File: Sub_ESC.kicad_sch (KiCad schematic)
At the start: 2 parts

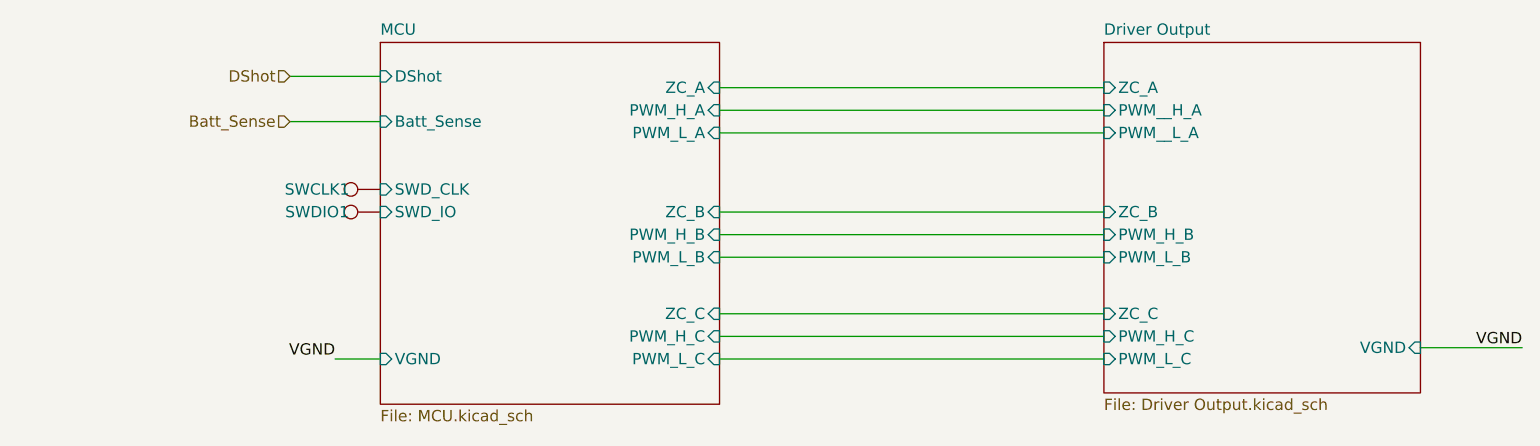
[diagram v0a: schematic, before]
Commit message: Fixed pin names
reset pins to apply proper net names
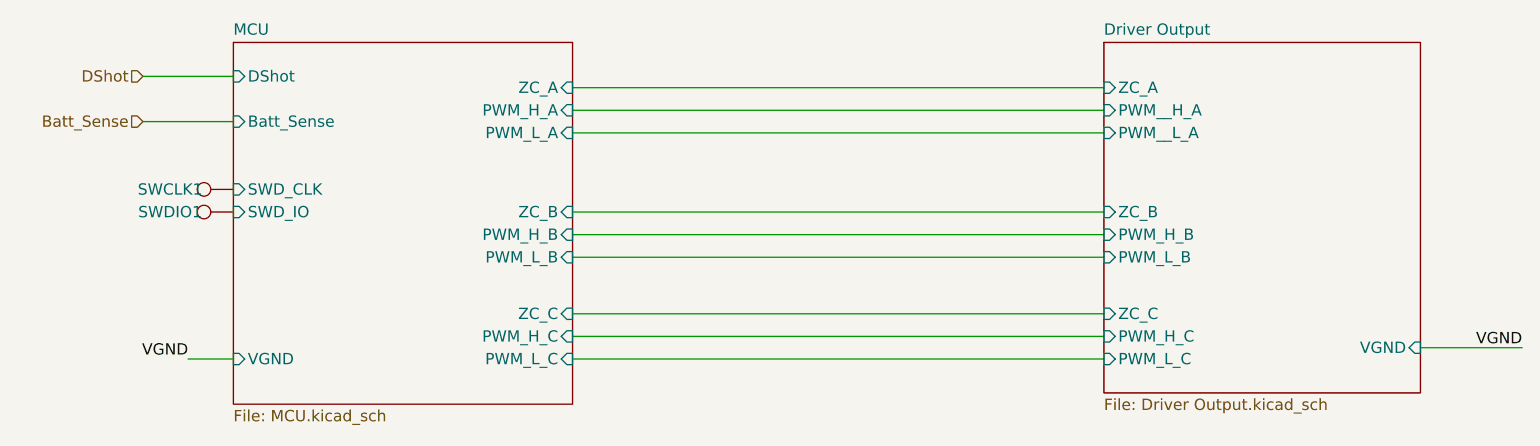
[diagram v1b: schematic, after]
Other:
- moved on the sheet: SWCLK1, SWDIO1
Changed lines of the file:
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@@
 	(wire
 		(pts
-			(xy 132.08 110.49) (xy 175.26 110.49)
-		)
-		(stroke
-			(width 0)
-			(type default)
-		)
-	)
-	(wire
-		(pts
-			(xy 132.08 82.55) (xy 175.26 82.55)
-		)
-		(stroke
-			(width 0)
-			(type default)
-		)
-	)
-	(wire
-		(pts
-			(xy 132.08 80.01) (xy 175.26 80.01)
-		)
-		(stroke
-			(width 0)
-			(type default)
-		)
-	)
-	(wire
-		(pts
-			(xy 132.08 85.09) (xy 175.26 85.09)
-		)
-		(stroke
-			(width 0)
-			(type default)
-		)
-	)
-	(wire
-		(pts
-			(xy 132.08 99.06) (xy 175.26 99.06)
-		)
-		(stroke
-			(width 0)
-			(type default)
-		)
-	)
-	(wire
-		(pts
-			(xy 132.08 105.41) (xy 175.26 105.41)
-		)
-		(stroke
-			(width 0)
-			(type default)
-		)
-	)
-	(wire
-		(pts
-			(xy 88.9 110.49) (xy 93.98 110.49)
-		)
-		(stroke
-			(width 0)
-			(type default)
-		)
-	)
-	(wire
-		(pts
-			(xy 132.08 96.52) (xy 175.26 96.52)
-		)
-		(stroke
-			(width 0)
-			(type default)
-		)
-	)
-	(wire
-		(pts
-			(xy 83.82 78.74) (xy 93.98 78.74)
-		)
-		(stroke
-			(width 0)
-			(type default)
-		)
-	)
-	(wire
-		(pts
-			(xy 132.08 107.95) (xy 175.26 107.95)
-		)
-		(stroke
-			(width 0)
-			(type default)
-		)
-	)
-	(wire
-		(pts
-			(xy 132.08 93.98) (xy 175.26 93.98)
-		)
-		(stroke
-			(width 0)
-			(type default)
-		)
-	)
-	(wire
-		(pts
-			(xy 83.82 83.82) (xy 93.98 83.82)
+			(xy 115.57 110.49) (xy 175.26 110.49)
+		)
+		(stroke
+			(width 0)
+			(type default)
+		)
+	)
+	(wire
+		(pts
+			(xy 115.57 82.55) (xy 175.26 82.55)
+		)
+		(stroke
+			(width 0)
+			(type default)
+		)
+	)
+	(wire
+		(pts
+			(xy 115.57 80.01) (xy 175.26 80.01)
+		)
+		(stroke
+			(width 0)
+			(type default)
+		)
+	)
+	(wire
+		(pts
+			(xy 115.57 85.09) (xy 175.26 85.09)
+		)
+		(stroke
+			(width 0)
+			(type default)
+		)
+	)
+	(wire
+		(pts
+			(xy 115.57 99.06) (xy 175.26 99.06)
+		)
+		(stroke
+			(width 0)
+			(type default)
+		)
+	)
+	(wire
+		(pts
+			(xy 115.57 105.41) (xy 175.26 105.41)
+		)
+		(stroke
+			(width 0)
+			(type default)
+		)
+	)
+	(wire
+		(pts
+			(xy 72.39 110.49) (xy 77.47 110.49)
+		)
+		(stroke
+			(width 0)
+			(type default)
+		)
+	)
+	(wire
+		(pts
+			(xy 115.57 96.52) (xy 175.26 96.52)
+		)
+		(stroke
+			(width 0)
+			(type default)
+		)
+	)
+	(wire
+		(pts
+			(xy 67.31 78.74) (xy 77.47 78.74)
+		)
+		(stroke
+			(width 0)
+			(type default)
+		)
+	)
+	(wire
+		(pts
+			(xy 115.57 107.95) (xy 175.26 107.95)
+		)
+		(stroke
+			(width 0)
+			(type default)
+		)
+	)
+	(wire
+		(pts
+			(xy 115.57 93.98) (xy 175.26 93.98)
+		)
+		(stroke
+			(width 0)
+			(type default)
+		)
+	)
+	(wire
+		(pts
+			(xy 67.31 83.82) (xy 77.47 83.82)
 		)
 		(stroke
@@
 	)
 	(label "VGND"
-		(at 88.9 110.49 180)
+		(at 72.39 110.49 180)
 		(effects
 			(font
@@
 	(hierarchical_label "DShot"
 		(shape input)
-		(at 83.82 78.74 180)
+		(at 67.31 78.74 180)
 		(effects
 			(font
@@
 	(hierarchical_label "Batt_Sense"
 		(shape input)
-		(at 83.82 83.82 180)
+		(at 67.31 83.82 180)
 		(effects
 			(font
@@
 	(symbol
 		(lib_id "Connector:TestPoint")
-		(at 93.98 91.44 90)
+		(at 77.47 91.44 90)
 		(unit 1)
 		(exclude_from_sim no)
@@
 		(dnp no)
 		(property "Reference" "SWCLK1"
-			(at 86.868 91.44 90)
+			(at 70.358 91.44 90)
 			(effects
 				(font
@@
 		)
 		(property "Value" "TestPoint"
-			(at 84.074 90.424 90)
+			(at 67.564 90.424 90)
 			(effects
 				(font
@@
 		)
 		(property "Footprint" "TestPoint:TestPoint_Pad_1.0x1.0mm"
-			(at 93.98 86.36 0)
+			(at 77.47 86.36 0)
 			(effects
 				(font
@@
 		)
 		(property "Datasheet" "~"
-			(at 93.98 86.36 0)
+			(at 77.47 86.36 0)
 			(effects
 				(font
@@
 		)
 		(property "Description" "test point"
-			(at 93.98 91.44 0)
+			(at 77.47 91.44 0)
 			(effects
 				(font
@@
 	(symbol
 		(lib_id "Connector:TestPoint")
-		(at 93.98 93.98 90)
+		(at 77.47 93.98 90)
 		(unit 1)
 		(exclude_from_sim no)
@@
 		(dnp no)
 		(property "Reference" "SWDIO1"
-			(at 86.868 93.98 90)
+			(at 70.358 93.98 90)
 			(effects
 				(font
@@
 		)
 		(property "Value" "TestPoint"
-			(at 90.678 91.44 90)
+			(at 74.168 91.44 90)
 			(effects
 				(font
@@
 		)
 		(property "Footprint" "TestPoint:TestPoint_Pad_1.0x1.0mm"
-			(at 93.98 88.9 0)
+			(at 77.47 88.9 0)
 			(effects
 				(font
@@
 		)
 		(property "Datasheet" "~"
-			(at 93.98 88.9 0)
+			(at 77.47 88.9 0)
 			(effects
 				(font
@@
 		)
 		(property "Description" "test point"
-			(at 93.98 93.98 0)
+			(at 77.47 93.98 0)
 			(effects
 				(font
@@
 	)
 	(sheet
-		(at 93.98 74.93)
+		(at 77.47 74.93)
 		(size 38.1 40.64)
 		(fields_autoplaced yes)
@@
 		)
 		(property "Sheetname" "MCU"
-			(at 93.98 74.2184 0)
+			(at 77.47 74.2184 0)
 			(effects
 				(font
@@
 		)
 		(property "Sheetfile" "MCU.kicad_sch"
-			(at 93.98 116.1546 0)
+			(at 77.47 116.1546 0)
 			(effects
 				(font
@@
 		)
 		(pin "Batt_Sense" input
-			(at 93.98 83.82 180)
+			(at 77.47 83.82 180)
 			(effects
 				(font
@@
 		)
 		(pin "ZC_B" input
-			(at 132.08 93.98 0)
+			(at 115.57 93.98 0)
 			(effects
 				(font
@@
 		)
 		(pin "ZC_C" input
-			(at 132.08 105.41 0)
+			(at 115.57 105.41 0)
 			(effects
 				(font
@@
 		)
 		(pin "ZC_A" input
-			(at 132.08 80.01 0)
+			(at 115.57 80.01 0)
 			(effects
 				(font
@@
 		)
 		(pin "SWD_IO" input
-			(at 93.98 93.98 180)
+			(at 77.47 93.98 180)
 			(effects
 				(font
@@
 		)
 		(pin "SWD_CLK" input
-			(at 93.98 91.44 180)
+			(at 77.47 91.44 180)
 			(effects
 				(font
@@
 		)
 		(pin "DShot" input
-			(at 93.98 78.74 180)
+			(at 77.47 78.74 180)
 			(effects
 				(font
@@
 		)
 		(pin "PWM_L_B" input
-			(at 132.08 99.06 0)
+			(at 115.57 99.06 0)
 			(effects
 				(font
@@
 		)
 		(pin "PWM_L_A" input
-			(at 132.08 85.09 0)
+			(at 115.57 85.09 0)
 			(effects
 				(font
@@
 		)
 		(pin "PWM_H_A" input
-			(at 132.08 82.55 0)
+			(at 115.57 82.55 0)
 			(effects
 				(font
@@
 		)
 		(pin "PWM_H_C" input
-			(at 132.08 107.95 0)
+			(at 115.57 107.95 0)
 			(effects
 				(font
@@
 		)
 		(pin "PWM_H_B" input
-			(at 132.08 96.52 0)
+			(at 115.57 96.52 0)
 			(effects
 				(font
@@
 		)
 		(pin "VGND" input
-			(at 93.98 110.49 180)
+			(at 77.47 110.49 180)
 			(effects
 				(font
@@
 		)
 		(pin "PWM_L_C" input
-			(at 132.08 110.49 0)
-			(effects
-				(font
+			(at 115.57 110.49 0)
+			(effects
+				(font

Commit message: more routing and placement
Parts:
- removed SWCLK1, SWDIO1: TestPoint, TestPoint:TestPoint_Pad_1.0x1.0mm, symbol Connector:TestPoint
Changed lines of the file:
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@@
+	(wire
+		(pts
+			(xy 73.66 93.98) (xy 77.47 93.98)
+		)
+		(stroke
+			(width 0)
+			(type default)
+		)
+	)
 	(wire
 		(pts
@@
 		(pts
 			(xy 115.57 105.41) (xy 175.26 105.41)
+		)
+		(stroke
+			(width 0)
+			(type default)
+		)
+	)
+	(wire
+		(pts
+			(xy 73.66 91.44) (xy 77.47 91.44)
 		)
 		(stroke
@@
 		)
 	)
+	(hierarchical_label "SWD_CLK_X"
+		(shape input)
+		(at 73.66 91.44 180)
+		(effects
+			(font
+				(size 1.27 1.27)
+			)
+			(justify right)
+		)
+	)
 	(hierarchical_label "Batt_Sense"
 		(shape input)
@@
 		)
 	)
-	(symbol
-		(lib_id "Connector:TestPoint")
-		(at 77.47 91.44 90)
-		(unit 1)
-		(exclude_from_sim no)
-		(in_bom yes)
-		(on_board yes)
-		(dnp no)
-		(property "Reference" "SWCLK1"
-			(at 70.358 91.44 90)
-			(effects
-				(font
-					(size 1.27 1.27)
-				)
-			)
-		)
-		(property "Value" "TestPoint"
-			(at 67.564 90.424 90)
-			(effects
-				(font
-					(size 1.27 1.27)
-				)
-				(hide yes)
-			)
-		)
-		(property "Footprint" "TestPoint:TestPoint_Pad_1.0x1.0mm"
-			(at 77.47 86.36 0)
-			(effects
-				(font
-					(size 1.27 1.27)
-				)
-				(hide yes)
-			)
-		)
-		(property "Datasheet" "~"
-			(at 77.47 86.36 0)
-			(effects
-				(font
-					(size 1.27 1.27)
-				)
-				(hide yes)
-			)
-		)
-		(property "Description" "test point"
-			(at 77.47 91.44 0)
-			(effects
-				(font
-					(size 1.27 1.27)
-				)
-				(hide yes)
-			)
-		)
-		(pin "1"
-		)
-		(instances
-			(project ""
-				(path "/0e826802-e676-4548-b85d-7973e5fc1500/dd4480c0-fc92-4865-b71a-49548ede0e1d"
-					(reference "SWCLK1")
-					(unit 1)
-				)
-			)
-		)
-	)
-	(symbol
-		(lib_id "Connector:TestPoint")
-		(at 77.47 93.98 90)
-		(unit 1)
-		(exclude_from_sim no)
-		(in_bom yes)
-		(on_board yes)
-		(dnp no)
-		(property "Reference" "SWDIO1"
-			(at 70.358 93.98 90)
-			(effects
-				(font
-					(size 1.27 1.27)
-				)
-			)
-		)
-		(property "Value" "TestPoint"
-			(at 74.168 91.44 90)
-			(effects
-				(font
-					(size 1.27 1.27)
-				)
-				(hide yes)
-			)
-		)
-		(property "Footprint" "TestPoint:TestPoint_Pad_1.0x1.0mm"
-			(at 77.47 88.9 0)
-			(effects
-				(font
-					(size 1.27 1.27)
-				)
-				(hide yes)
-			)
-		)
-		(property "Datasheet" "~"
-			(at 77.47 88.9 0)
-			(effects
-				(font
-					(size 1.27 1.27)
-				)
-				(hide yes)
-			)
-		)
-		(property "Description" "test point"
-			(at 77.47 93.98 0)
-			(effects
-				(font
-					(size 1.27 1.27)
-				)
-				(hide yes)
-			)
-		)
-		(pin "1"
-		)
-		(instances
-			(project ""
-				(path "/0e826802-e676-4548-b85d-7973e5fc1500/dd4480c0-fc92-4865-b71a-49548ede0e1d"
-					(reference "SWDIO1")
-					(unit 1)
-				)
-			)
+	(hierarchical_label "SWD_IO_X"
+		(shape input)
+		(at 73.66 93.98 180)
+		(effects
+			(font
+				(size 1.27 1.27)
+			)
+			(justify right)
 		)
 	)
@@
 					(page "3")
 				)
+				(path "/0e826802-e676-4548-b85d-7973e5fc1500/67868d63-a0ad-4135-884b-a4305faec098"
+					(page "10")
+				)
+				(path "/0e826802-e676-4548-b85d-7973e5fc1500/f0f91033-e6f6-4ba6-a242-b2d52399ba4f"
+					(page "16")
+				)
+				(path "/0e826802-e676-4548-b85d-7973e5fc1500/e90d83da-778a-41e9-b4cb-1e16efdba290"
+					(page "22")
+				)
 			)
 		)
@@
 					(page "7")
 				)
-			)
+				(path "/0e826802-e676-4548-b85d-7973e5fc1500/67868d63-a0ad-4135-884b-a4305faec098"
+					(page "14")
+				)
+				(path "/0e826802-e676-4548-b85d-7973e5fc1500/f0f91033-e6f6-4ba6-a242-b2d52399ba4f"
+					(page "20")
+				)
+				(path "/0e826802-e676-4548-b85d-7973e5fc1500/e90d83da-778a-41e9-b4cb-1e16efdba290"
+					(page "26")
+				)
+			)
